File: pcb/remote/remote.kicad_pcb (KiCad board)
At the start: 2 copper layers, 27 x 29 mm, 9 parts, among them J1 Conn_01x07_Female

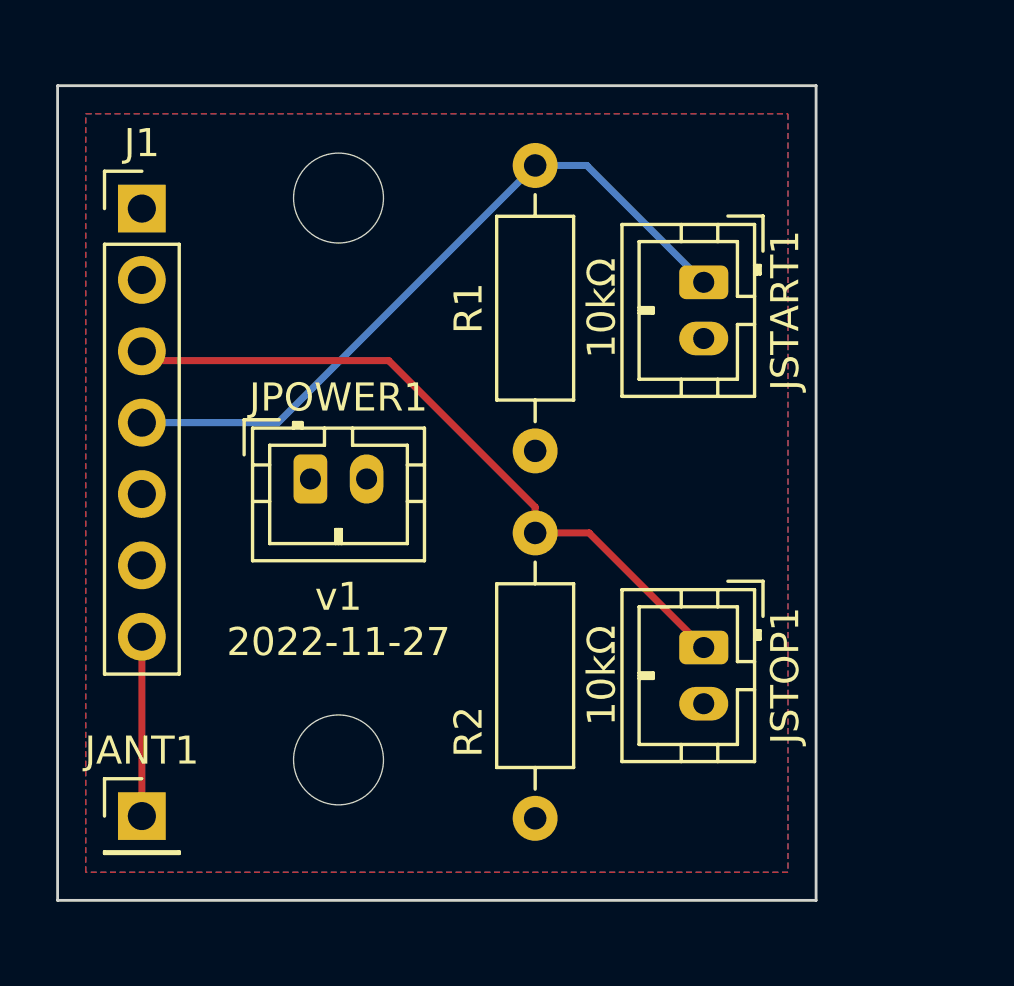
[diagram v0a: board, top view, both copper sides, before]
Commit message: Remote PCB Update
This updates the remote control PCB to use tactile switches directly
on the board instead of buttons connected via JST connector.
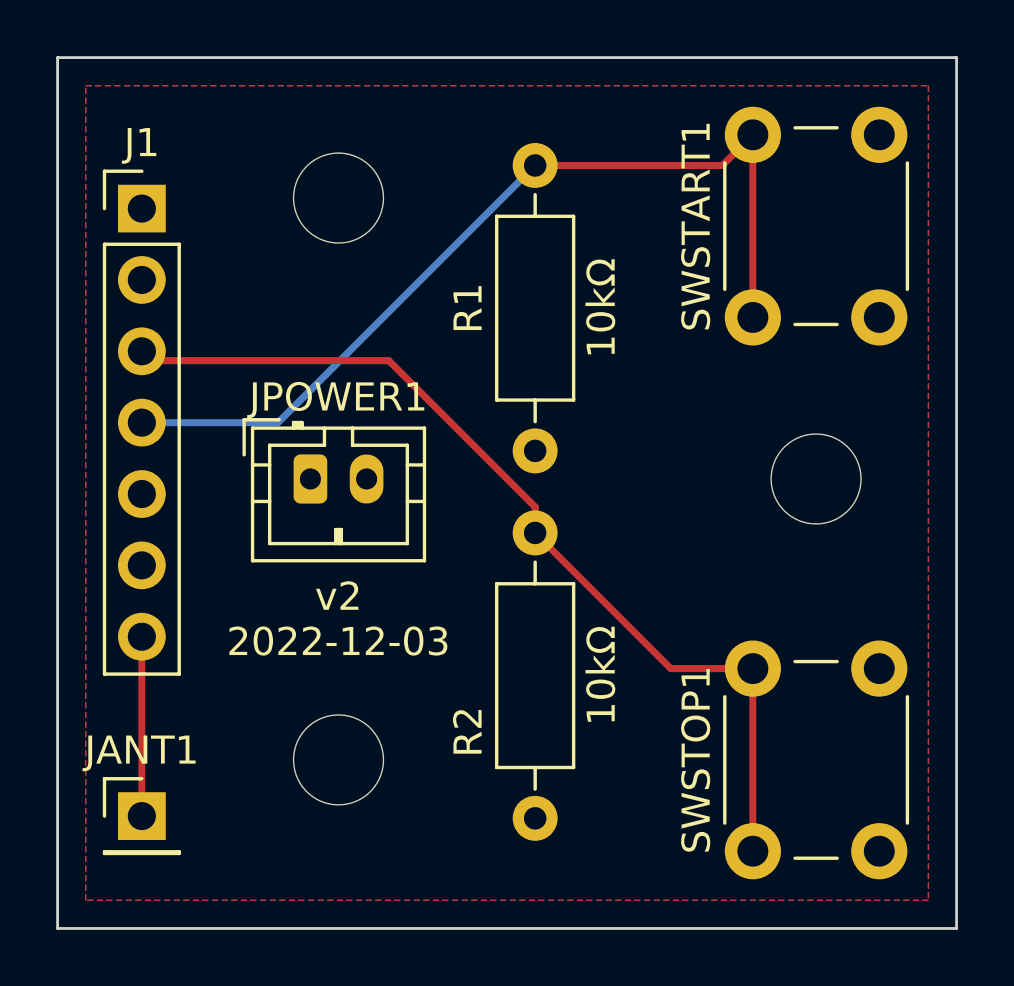
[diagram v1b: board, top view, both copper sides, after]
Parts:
- removed JSTART1, JSTOP1: Conn_01x02_Female, Connector_JST:JST_PH_B2B-PH-K_1x02_P2.00mm_Vertical
- added REF**: MountingHole_3.2mm_M3, MountingHole:MountingHole_3.2mm_M3, F.Cu at (159.0, 78.0)
- added SWSTART1: SW_Push, Button_Switch_THT:SW_PUSH_6mm, F.Cu at (156.8, 72.2)
- added SWSTOP1: SW_Push, Button_Switch_THT:SW_PUSH_6mm, F.Cu at (156.8, 91.2)
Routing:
- net Net-(J1-Pad3): track 25.1 -> 33.7 mm
- net Net-(J1-Pad4): track 25.5 -> 32.5 mm
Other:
- board size 27 x 29 mm -> 32 x 31 mm
- board text added: "v2 2022-12-03"
- board text removed: "v1 2022-11-27"
